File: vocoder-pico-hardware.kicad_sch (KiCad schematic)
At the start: 29 parts, among them SW1 SW_Push, SW2 SW_Push, U1 PCM5100A

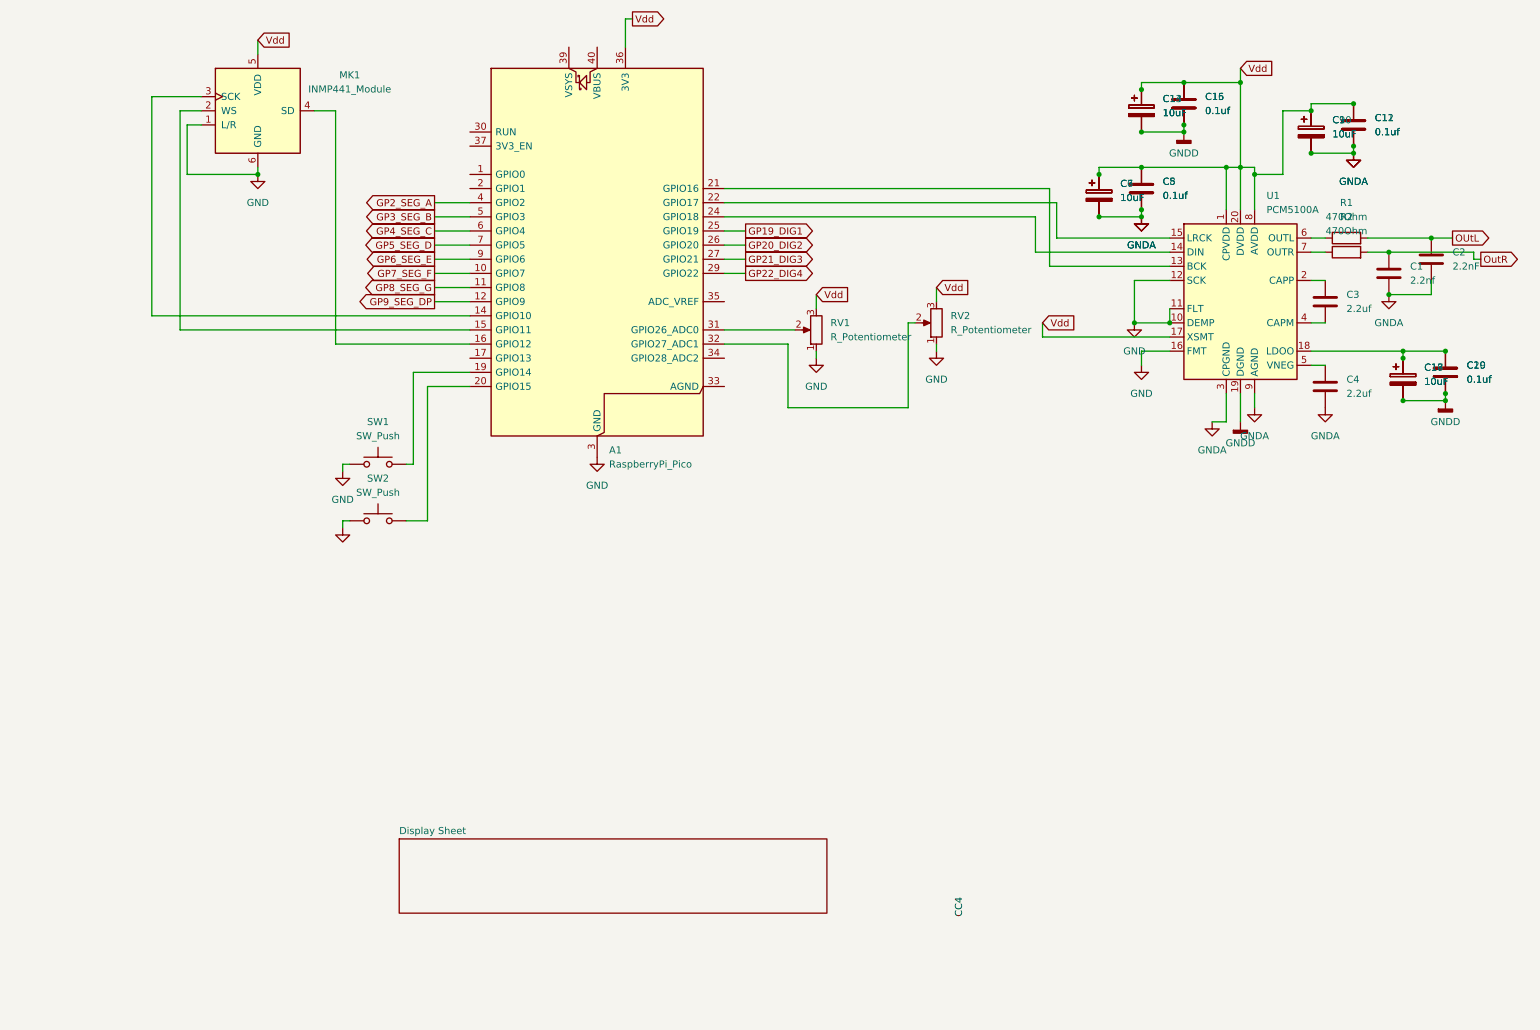
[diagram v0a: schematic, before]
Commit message: add output amplifier
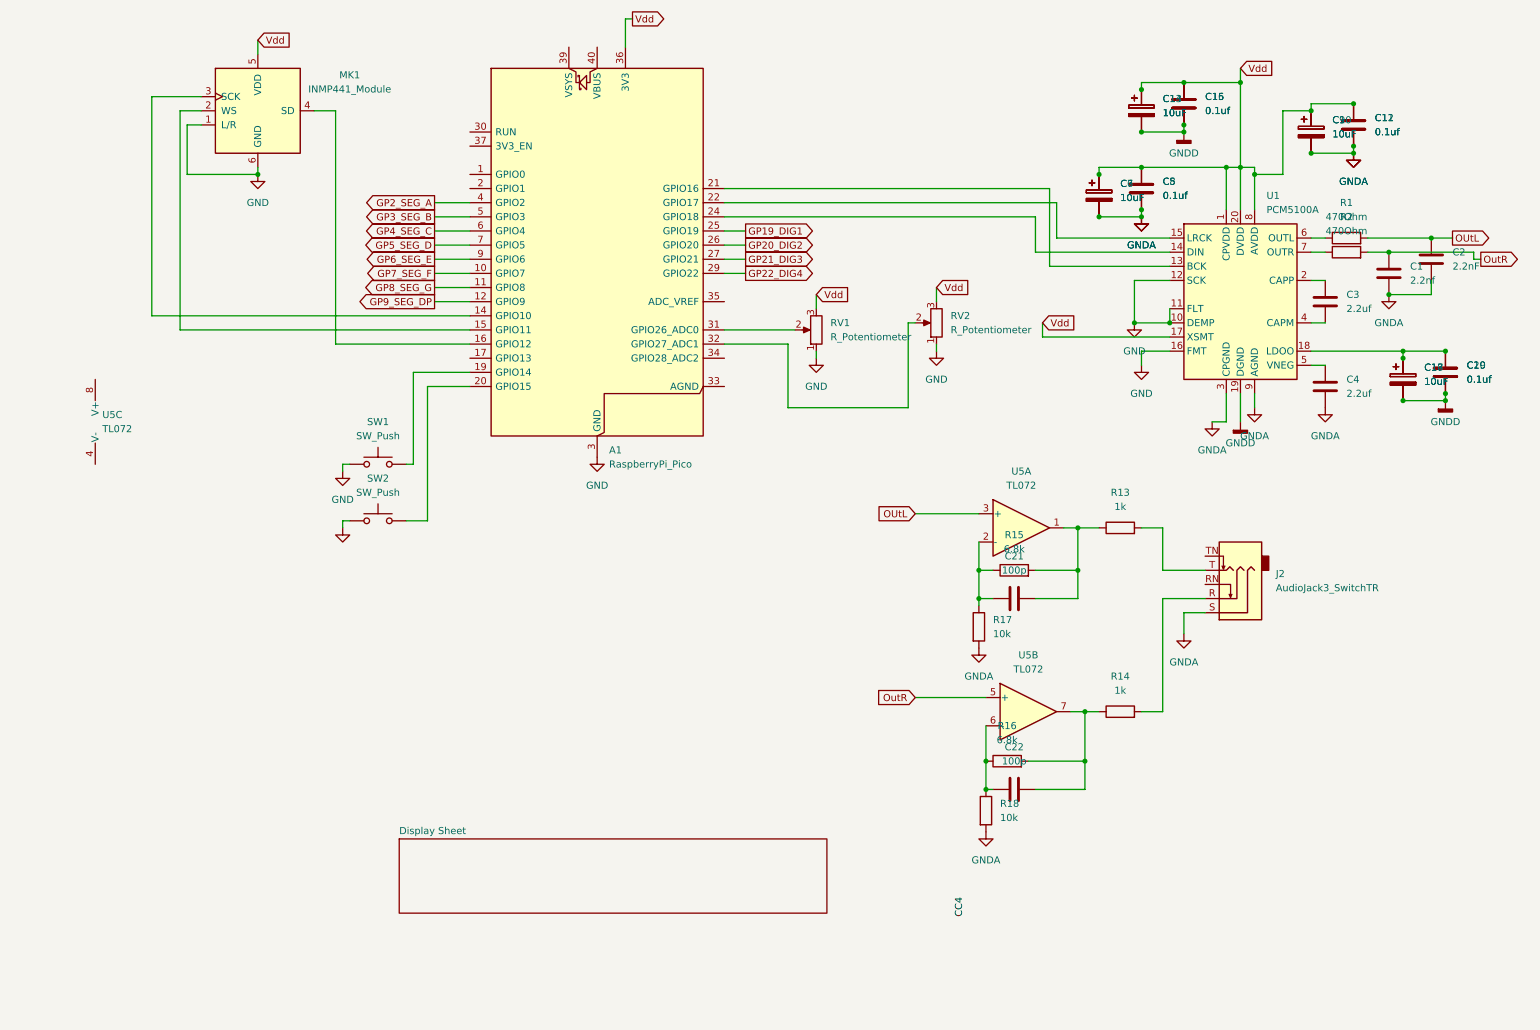
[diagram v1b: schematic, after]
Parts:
- added C21, C22: 100p, symbol Device:C
- added J2: AudioJack3_SwitchTR, symbol Connector_Audio:AudioJack3_SwitchTR
- added R13, R14: 1k, symbol Device:R
- added R15, R16: 6.8k, symbol Device:R
- added R17, R18: 10k, symbol Device:R
- added U5: TL072, symbol Amplifier_Operational:TL072
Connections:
- net GNDA: now also J2.S, R17.2, R18.2
- net OUtL: now also U5.3 (+)
- net OutR: now also U5.5 (+)
- new net: C21.1, R15.1, R17.1, U5.2 (-)
- new net: C21.2, R13.1, R15.2, U5.1
- new net: C22.2, R14.1, R16.2, U5.7
- new net: J2.R, R14.2
- new net: C22.1, R16.1, R18.1, U5.6 (-)
- new net: J2.T, R13.2

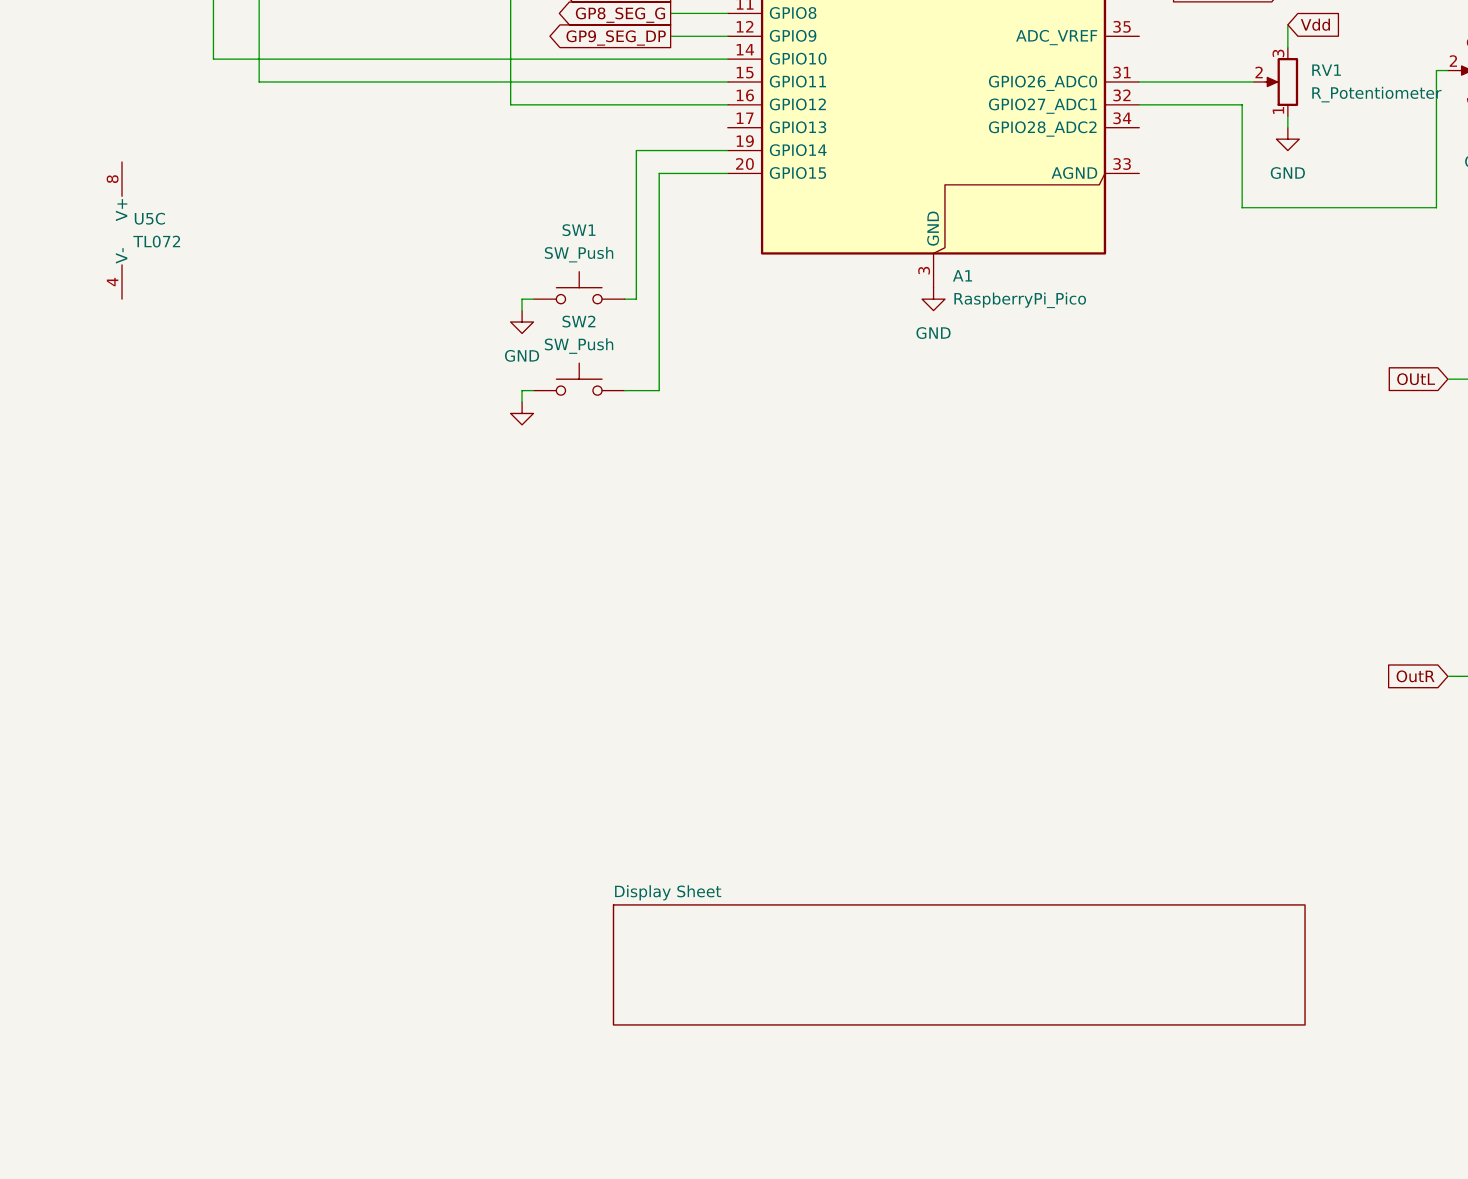
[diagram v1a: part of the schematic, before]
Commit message: add power supply
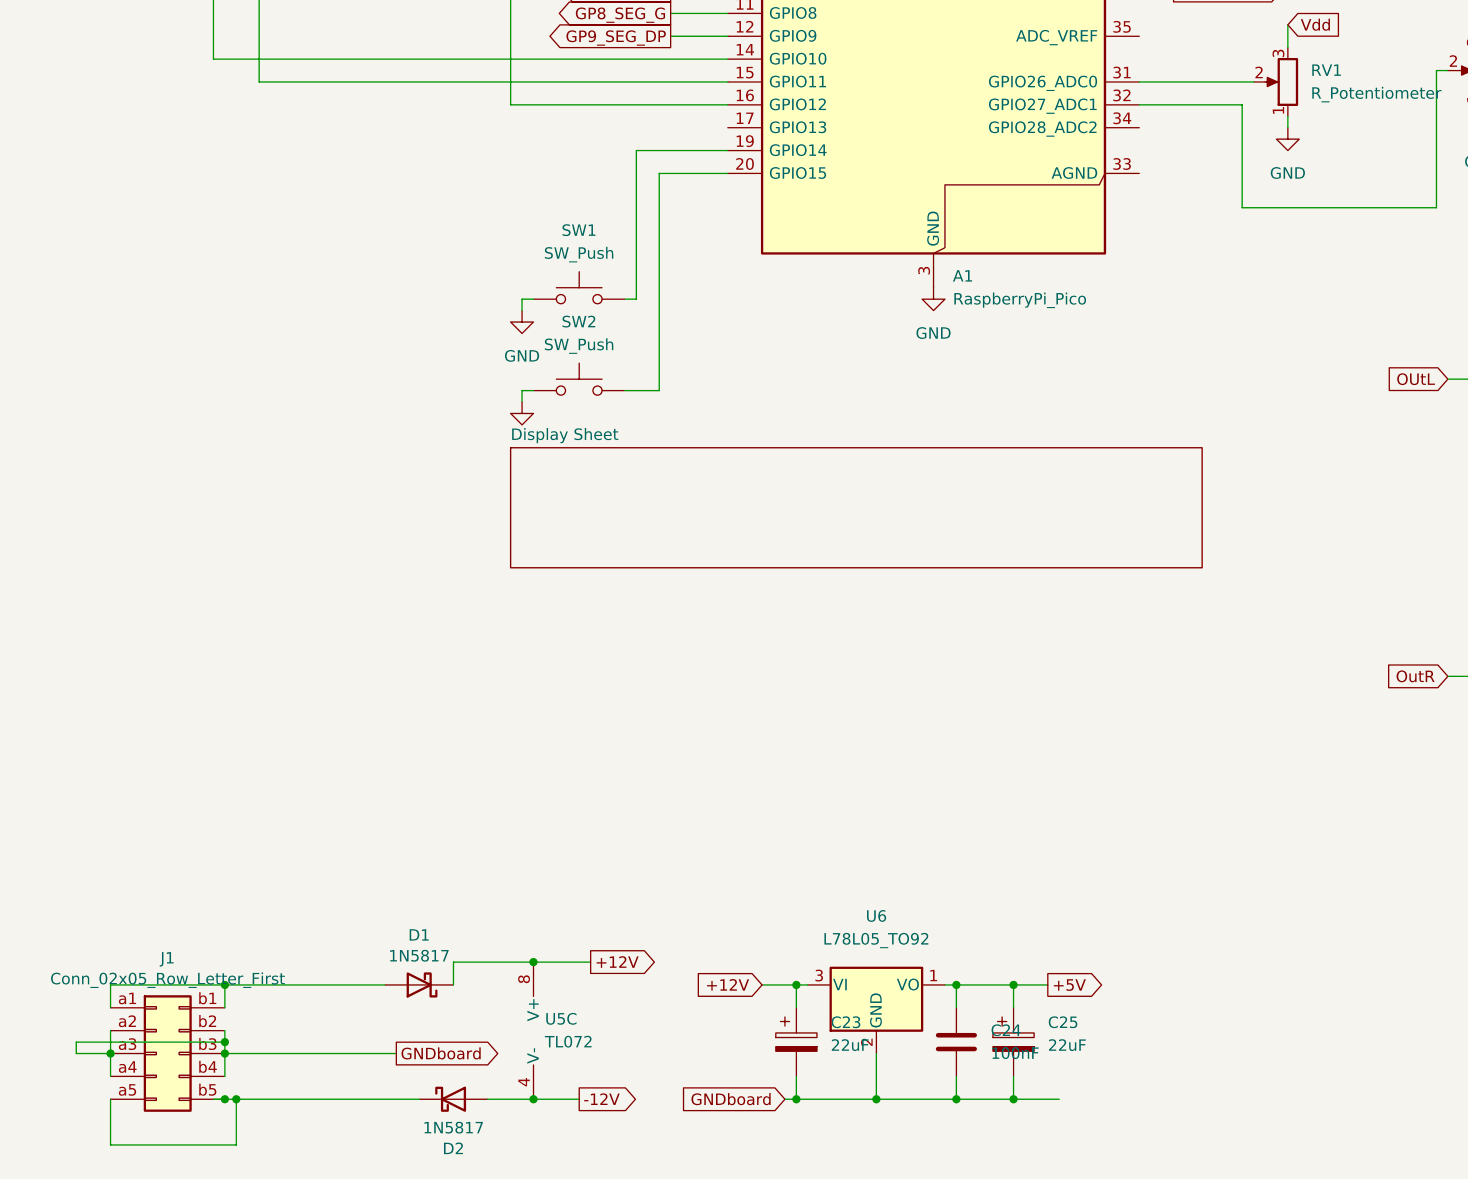
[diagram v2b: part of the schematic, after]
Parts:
- added C23, C25: 22uF, Capacitor_THT:CP_Radial_D8.0mm_P3.80mm, symbol Device:C_Polarized
- added C24: 100nF, Capacitor_THT:C_Disc_D5.0mm_W2.5mm_P5.00mm, symbol Device:C
- added D1, D2: 1N5817, Diode_THT:D_DO-41_SOD81_P10.16mm_Horizontal, symbol Diode:1N5817
- added J1: Conn_02x05_Row_Letter_First, Connector_PinHeader_2.54mm:PinHeader_2x05_P2.54mm_Vertical, symbol Connector_Generic:Conn_02x05_Row_Letter_First
- added U6: L78L05_TO92, Package_TO_SOT_THT:TO-92_Inline, symbol Regulator_Linear:L78L05_TO92
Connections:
- net -12V: now reaches U5.4 (V-)
- net -12V: now also D2.2 (A)
- net +12V: now reaches U5.8 (V+)
- net +12V: now also C23.1, D1.1 (K), U6.3 (VI)
- new net: D1.2 (A), J1.a1 (Pin_a1), J1.b1 (Pin_b1)
- new net: D2.1 (K), J1.a5 (Pin_a5), J1.b5 (Pin_b5)
- new net +5V: C24.1, C25.1, U6.1 (VO)
- new net GNDboard: C23.2, C24.2, C25.2, J1.a2 (Pin_a2), J1.a3 (Pin_a3), J1.a4 (Pin_a4), J1.b2 (Pin_b2), J1.b3 (Pin_b3), J1.b4 (Pin_b4), U6.2 (GND)
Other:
- moved on the sheet: U5C

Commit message: fix errors in power supply
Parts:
- removed J1: Conn_02x05_Row_Letter_First, Connector_PinHeader_2.54mm:PinHeader_2x05_P2.54mm_Vertical, symbol Connector_Generic:Conn_02x05_Row_Letter_First
- removed U6: L78L05_TO92, Package_TO_SOT_THT:TO-92_Inline, symbol Regulator_Linear:L78L05_TO92
- added D3: 1N5817, Diode_THT:D_DO-41_SOD81_P10.16mm_Horizontal, symbol Diode:1N5817
- added J1: Conn_02x05_Odd_Even, symbol Connector_Generic:Conn_02x05_Odd_Even
- added U7: LM7805_TO220, Package_TO_SOT_THT:TO-220-3_Vertical, symbol Regulator_Linear:LM7805_TO220
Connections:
- net GNDA is gone; now on net GND: C1.2, C10.2, C11.2, C12.2, C2.2, C4.2, C5.2, C6.2, C7.2, C8.2, C9.2, J2.S, R17.2, R18.2, U1.3 (CPGND), U1.9 (AGND)
- net GNDD is gone; now on net GND: C13.2, C14.2, C15.2, C16.2, C17.2, C18.2, C19.2, C20.2, U1.19 (DGND)
- net GNDboard is gone; now on net GND: C23.2, C24.2, C25.2
- net +12V: now also U7.1 (VI)
- net +5V: now also D3.2 (A), U7.3 (VO)
- net GND: now also J1.3 (Pin_3), J1.4 (Pin_4), J1.5 (Pin_5), J1.6 (Pin_6), J1.7 (Pin_7), J1.8 (Pin_8), U7.2 (GND)
- net at D1.2 (A): now also J1.10 (Pin_10), J1.9 (Pin_9)
- net at D2.1 (K): now also J1.1 (Pin_1), J1.2 (Pin_2)
- net Vsys: now reaches A1.39 (VSYS)
- net Vsys: now also D3.1 (K)

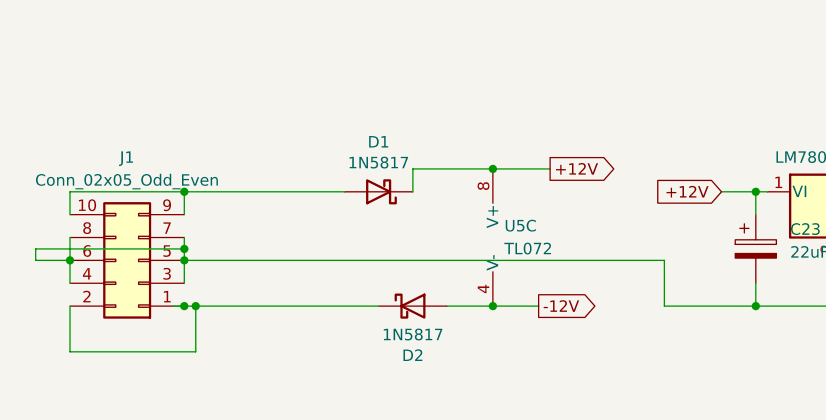
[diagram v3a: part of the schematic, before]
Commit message: improve power supply
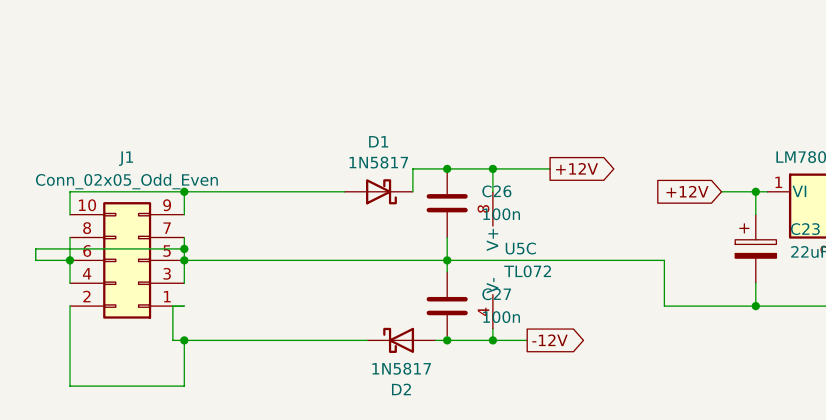
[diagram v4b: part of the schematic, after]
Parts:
- added C26, C27: 100n, symbol Device:C
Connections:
- net +12V: now also C26.1
- net -12V: now also C27.2
- net GND: now also C26.2, C27.1
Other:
- moved on the sheet: D2, U5C

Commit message: correcting ic numbers
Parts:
- added C28: 22uF, Capacitor_THT:CP_Radial_D8.0mm_P3.80mm, symbol Device:C_Polarized
- renumbered U1 to U6
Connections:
- net -12V: now also C28.2
- net GND: now also C28.1
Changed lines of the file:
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@@
 	)
 	(junction
+		(at 82.55 189.23)
+		(diameter 0)
+		(color 0 0 0 0)
+	)
+	(junction
 		(at 207.01 149.86)
 		(diameter 0)
@@
 	)
 	(junction
+		(at 82.55 180.34)
+		(diameter 0)
+		(color 0 0 0 0)
+	)
+	(junction
 		(at 264.16 85.09)
 		(diameter 0)
@@
 	(wire
 		(pts
-			(xy 74.93 189.23) (xy 78.74 189.23)
+			(xy 74.93 189.23) (xy 82.55 189.23)
 		)
 		(stroke
@@
 	(wire
 		(pts
+			(xy 82.55 180.34) (xy 93.98 180.34)
+		)
+		(stroke
+			(width 0)
+			(type default)
+		)
+	)
+	(wire
+		(pts
 			(xy 217.17 29.21) (xy 217.17 27.94)
 		)
@@
 	(wire
 		(pts
-			(xy 69.85 180.34) (xy 93.98 180.34)
+			(xy 69.85 180.34) (xy 82.55 180.34)
 		)
 		(stroke
@@
 	(wire
 		(pts
+			(xy 82.55 181.61) (xy 82.55 180.34)
+		)
+		(stroke
+			(width 0)
+			(type default)
+		)
+	)
+	(wire
+		(pts
 			(xy 74.93 170.18) (xy 81.28 170.18)
 		)
@@
 	(wire
 		(pts
+			(xy 82.55 189.23) (xy 85.09 189.23)
+		)
+		(stroke
+			(width 0)
+			(type default)
+		)
+	)
+	(wire
+		(pts
 			(xy 24.13 180.34) (xy 24.13 179.07)
 		)
@@
 	(global_label "-12V"
 		(shape output)
-		(at 78.74 189.23 0)
+		(at 85.09 189.23 0)
 		(fields_autoplaced yes)
 		(effects
@@
 		)
 		(property "Intersheetrefs" "${INTERSHEET_REFS}"
-			(at 86.1442 189.1506 0)
+			(at 92.4942 189.1506 0)
 			(effects
 				(font
@@
 		(dnp no)
 		(fields_autoplaced yes)
-		(property "Reference" "U1"
+		(property "Reference" "U6"
 			(at 239.6333 48.26 0)
 			(effects
@@
 			(project "vocoder-pico-hardware"
 				(path "/68f2073a-7618-4fa5-a11d-b71bb4f75794"
-					(reference "U1")
+					(reference "U6")
 					(unit 1)
 				)
@@
 					(unit 1)
 				)
+			)
+		)
+	)
+	(symbol
+		(lib_id "Device:C_Polarized")
+		(at 82.55 185.42 0)
+		(unit 1)
+		(exclude_from_sim no)
+		(in_bom yes)
+		(on_board yes)
+		(dnp no)
+		(fields_autoplaced yes)
+		(property "Reference" "C28"
+			(at 86.36 183.2609 0)
+			(effects
+				(font
+					(size 1.27 1.27)
+				)
+				(justify left)
+			)
+		)
+		(property "Value" "22uF"
+			(at 86.36 185.8009 0)
+			(effects
+				(font
+					(size 1.27 1.27)
+				)
+				(justify left)
+			)
+		)
+		(property "Footprint" "Capacitor_THT:CP_Radial_D8.0mm_P3.80mm"
+			(at 83.5152 189.23 0)
+			(effects
+				(font
+					(size 1.27 1.27)
+				)
+				(hide yes)
+			)
+		)
+		(property "Datasheet" "~"
+			(at 82.55 185.42 0)
+			(effects
+				(font
+					(size 1.27 1.27)
+				)
+				(hide yes)
+			)
+		)
+		(property "Description" ""
+			(at 82.55 185.42 0)
+			(effects
+				(font
+					(size 1.27 1.27)
+				)
+				(hide yes)
+			)
+		)
+		(pin "1"
+		)
+		(pin "2"
+		)
+		(instances
+			(project "vocoder-pico-hardware"
+				(path "/68f2073a-7618-4fa5-a11d-b71bb4f75794"
+					(reference "C28")
+					(unit 1)
+				)

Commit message: reset annotations
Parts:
- renumbered C26 to C1, C6 to C10, C13 to C11, C14 to C12, C8 to C13, C5 to C14, C9 to C17, C10 to C18, C3 to C19, C27 to C2, C4 to C20, C11 to C21, C12 to C22, C1 to C23, C17 to C24, C18 to C25, C2 to C26, C19 to C27, C20 to C28, C28 to C3, C23 to C4, C24 to C5, C25 to C6, C21 to C7, C22 to C8, C7 to C9, R17 to R1, R18 to R2, R16 to R3, R15 to R4, R13 to R5, R14 to R6, R1 to R7, R2 to R8, U5 to U1, U7 to U2, U6 to U3

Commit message: remove duplicates
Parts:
- removed C10, C11, C18, C24: 10uF, symbol Device:C_Polarized
- removed C13, C16, C21, C27: 0.1uf, symbol Device:C
